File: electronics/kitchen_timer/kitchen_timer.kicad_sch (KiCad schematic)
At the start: 25 parts, among them J2 UART, J3 SWD, Q1 BC327, Q2 BC327, Q3 BC327, Q4 BC327, SW1 BTN_A, SW2 BTN_B, SW3 BTN_C, SW4 BTN_D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

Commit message: Add 3d models to components, small rerouting
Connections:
- net GND: now also U2.23 (GND), U2.28 (GND)
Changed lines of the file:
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@@
+	)
+	(junction
+		(at 121.92 64.77)
+		(diameter 0)
+		(color 0 0 0 0)
 	)
 	(junction
@@
 	)
 	(junction
+		(at 121.92 39.37)
+		(diameter 0)
+		(color 0 0 0 0)
+	)
+	(junction
 		(at 33.02 69.85)
 		(diameter 0)
@@
 	(wire
 		(pts
+			(xy 121.92 77.47) (xy 121.92 64.77)
+		)
+		(stroke
+			(width 0)
+			(type default)
+		)
+	)
+	(wire
+		(pts
 			(xy 39.37 69.85) (xy 45.72 69.85)
 		)
@@
 	(wire
 		(pts
+			(xy 121.92 64.77) (xy 121.92 39.37)
+		)
+		(stroke
+			(width 0)
+			(type default)
+		)
+	)
+	(wire
+		(pts
 			(xy 191.77 120.65) (xy 191.77 161.29)
 		)
@@
 	(wire
 		(pts
-			(xy 129.54 39.37) (xy 118.11 39.37)
+			(xy 129.54 39.37) (xy 121.92 39.37)
 		)
 		(stroke
@@
 	(wire
 		(pts
+			(xy 121.92 39.37) (xy 118.11 39.37)
+		)
+		(stroke
+			(width 0)
+			(type default)
+		)
+	)
+	(wire
+		(pts
 			(xy 106.68 157.48) (xy 106.68 181.61)
 		)
@@
 	(wire
 		(pts
+			(xy 118.11 77.47) (xy 121.92 77.47)
+		)
+		(stroke
+			(width 0)
+			(type default)
+		)
+	)
+	(wire
+		(pts
 			(xy 163.83 44.45) (xy 173.99 44.45)
 		)
@@
 		)
 		(stroke
+			(width 0)
+			(type default)
+		)
+	)
+	(wire
+		(pts
+			(xy 118.11 64.77) (xy 121.92 64.77)
+		)
+		(stroke

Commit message: Update electronics
- added Schottky diode and solder bridge
- corrected all errors from design rules checker
- added silk screen logos
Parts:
- added TP1: PWM_SPEAKER, TestPoint:TestPoint_Pad_2.0x2.0mm, symbol Connector:TestPoint
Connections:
- net GND: now also U2.13 (GND), U2.18 (GND), U2.8 (GND)
- net charging_and_audio/PWM_SPEAKER renamed PWM_SPEAKER
- net PWM_SPEAKER: now also TP1.1
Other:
- note added: "Testpoints"
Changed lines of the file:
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@@
 	)
 	(junction
+		(at 67.31 39.37)
+		(diameter 0)
+		(color 0 0 0 0)
+	)
+	(junction
 		(at 121.92 64.77)
 		(diameter 0)
@@
 	)
 	(junction
+		(at 80.01 64.77)
+		(diameter 0)
+		(color 0 0 0 0)
+	)
+	(junction
 		(at 121.92 39.37)
 		(diameter 0)
@@
 	)
 	(junction
+		(at 76.2 52.07)
+		(diameter 0)
+		(color 0 0 0 0)
+	)
+	(junction
 		(at 173.99 44.45)
 		(diameter 0)
@@
 	(wire
 		(pts
+			(xy 76.2 64.77) (xy 76.2 52.07)
+		)
+		(stroke
+			(width 0)
+			(type default)
+		)
+	)
+	(wire
+		(pts
 			(xy 95.25 116.84) (xy 119.38 116.84)
 		)
@@
 	(wire
 		(pts
+			(xy 76.2 52.07) (xy 67.31 52.07)
+		)
+		(stroke
+			(width 0)
+			(type default)
+		)
+	)
+	(wire
+		(pts
 			(xy 58.42 59.69) (xy 58.42 57.15)
 		)
@@
 	(wire
 		(pts
+			(xy 67.31 39.37) (xy 82.55 39.37)
+		)
+		(stroke
+			(width 0)
+			(type default)
+		)
+	)
+	(wire
+		(pts
 			(xy 101.6 99.06) (xy 101.6 138.43)
 		)
@@
 	(wire
 		(pts
-			(xy 118.11 54.61) (xy 146.05 54.61)
-		)
-		(stroke
-			(width 0)
-			(type default)
-		)
-	)
-	(wire
-		(pts
 			(xy 115.57 130.81) (xy 115.57 138.43)
 		)
@@
 	(wire
 		(pts
+			(xy 223.52 30.48) (xy 229.87 30.48)
+		)
+		(stroke
+			(width 0)
+			(type default)
+		)
+	)
+	(wire
+		(pts
 			(xy 73.66 172.72) (xy 82.55 172.72)
 		)
@@
 	(wire
 		(pts
+			(xy 80.01 64.77) (xy 76.2 64.77)
+		)
+		(stroke
+			(width 0)
+			(type default)
+		)
+	)
+	(wire
+		(pts
 			(xy 134.62 83.82) (xy 134.62 105.41)
 		)
@@
 	(wire
 		(pts
+			(xy 82.55 64.77) (xy 80.01 64.77)
+		)
+		(stroke
+			(width 0)
+			(type default)
+		)
+	)
+	(wire
+		(pts
+			(xy 80.01 77.47) (xy 80.01 64.77)
+		)
+		(stroke
+			(width 0)
+			(type default)
+		)
+	)
+	(wire
+		(pts
 			(xy 182.88 130.81) (xy 115.57 130.81)
 		)
@@
 	(wire
 		(pts
+			(xy 67.31 52.07) (xy 67.31 39.37)
+		)
+		(stroke
+			(width 0)
+			(type default)
+		)
+	)
+	(wire
+		(pts
 			(xy 182.88 44.45) (xy 182.88 100.33)
 		)
@@
 	(wire
 		(pts
+			(xy 118.11 54.61) (xy 157.48 54.61)
+		)
+		(stroke
+			(width 0)
+			(type default)
+		)
+	)
+	(wire
+		(pts
 			(xy 45.72 69.85) (xy 58.42 69.85)
 		)
@@
 	(wire
 		(pts
-			(xy 146.05 31.75) (xy 165.1 31.75)
+			(xy 157.48 31.75) (xy 165.1 31.75)
 		)
 		(stroke
@@
 	(wire
 		(pts
+			(xy 157.48 31.75) (xy 157.48 54.61)
+		)
+		(stroke
+			(width 0)
+			(type default)
+		)
+	)
+	(wire
+		(pts
 			(xy 66.04 59.69) (xy 66.04 92.71)
 		)
@@
 	(wire
 		(pts
-			(xy 66.04 92.71) (xy 44.45 92.71)
+			(xy 82.55 52.07) (xy 76.2 52.07)
 		)
 		(stroke
@@
 	(wire
 		(pts
-			(xy 39.37 69.85) (xy 39.37 77.47)
+			(xy 66.04 92.71) (xy 44.45 92.71)
 		)
 		(stroke
@@
 	(wire
 		(pts
-			(xy 146.05 54.61) (xy 146.05 31.75)
+			(xy 39.37 69.85) (xy 39.37 77.47)
 		)
 		(stroke
@@
 	(wire
 		(pts
+			(xy 82.55 77.47) (xy 80.01 77.47)
+		)
+		(stroke
+			(width 0)
+			(type default)
+		)
+	)
+	(wire
+		(pts
 			(xy 90.17 172.72) (xy 111.76 172.72)
 		)
@@
 	(wire
 		(pts
-			(xy 57.15 39.37) (xy 82.55 39.37)
+			(xy 57.15 39.37) (xy 67.31 39.37)
 		)
 		(stroke
@@
 	(wire
 		(pts
+			(xy 223.52 27.94) (xy 223.52 30.48)
+		)
+		(stroke
+			(width 0)
+			(type default)
+		)
+	)
+	(wire
+		(pts
 			(xy 33.02 49.53) (xy 33.02 59.69)
 		)
@@
 		)
 	)
+	(rectangle
+		(start 218.44 20.32)
+		(end 274.32 33.02)
+		(stroke
+			(width 0)
+			(type default)
+		)
+		(fill
+			(type color)
+			(color 255 255 175 1)
+		)
+	)
 	(image
 		(at 243.84 147.32)
@@
 		)
 	)
-	(text_box "TODO\n- Zener diode"
+	(text "Segments and digits:"
 		(exclude_from_sim no)
-		(at 215.9 85.09 0)
-		(size 54.61 25.4)
-		(stroke
-			(width 0)
-			(type default)
+		(at 244.348 132.842 0)
+		(effects
+			(font
+				(size 1.27 1.27)
+			)
 		)
-		(fill
-			(type color)
-			(color 255 255 175 1)
+	)
+	(text "Testpoints"
+		(exclude_from_sim no)
+		(at 245.11 18.034 0)
+		(effects
+			(font
+				(size 1.27 1.27)
+			)
 		)
+	)
+	(label "PWM_SPEAKER"
+		(at 229.87 30.48 0)
+		(fields_autoplaced yes)
 		(effects
 			(font
 				(size 1.27 1.27)
 			)
-			(justify left top)
+			(justify left bottom)
 		)
 	)
-	(text "Segments and digits:"
-		(exclude_from_sim no)
-		(at 244.348 132.842 0)
+	(label "PWM_SPEAKER"
+		(at 135.89 54.61 0)
+		(fields_autoplaced yes)
 		(effects
 			(font
 				(size 1.27 1.27)
 			)
+			(justify left bottom)
 		)
 	)
@@
 					(unit 1)
 				)
+			)
+		)
+	)
+	(symbol
+		(lib_id "Connector:TestPoint")
+		(at 223.52 27.94 0)
+		(unit 1)
+		(exclude_from_sim no)
+		(in_bom yes)
+		(on_board yes)
+		(dnp no)
+		(fields_autoplaced yes)
+		(property "Reference" "TP1"
+			(at 226.06 23.3679 0)
+			(effects
+				(font
+					(size 1.27 1.27)
+				)
+				(justify left)
+			)
+		)
+		(property "Value" "PWM_SPEAKER"
+			(at 226.06 25.9079 0)
+			(effects
+				(font
+					(size 1.27 1.27)
+				)
+				(justify left)
+			)
+		)
+		(property "Footprint" "TestPoint:TestPoint_Pad_2.0x2.0mm"
+			(at 228.6 27.94 0)
+			(effects
+				(font
+					(size 1.27 1.27)
+				)
+				(hide yes)
+			)
+		)
+		(property "Datasheet" "~"
+			(at 228.6 27.94 0)
+			(effects
+				(font
+					(size 1.27 1.27)
+				)
+				(hide yes)
+			)
+		)
+		(property "Description" "test point"
+			(at 223.52 27.94 0)
+			(effects
+				(font
+					(size 1.27 1.27)
+				)
+				(hide yes)
+			)
+		)
+		(pin "1"
+		)
+		(instances
+			(project ""
+				(path "/10a34ff8-9938-4755-8ae4-3799cb1684e2"
+					(reference "TP1")
+					(unit 1)
+				)

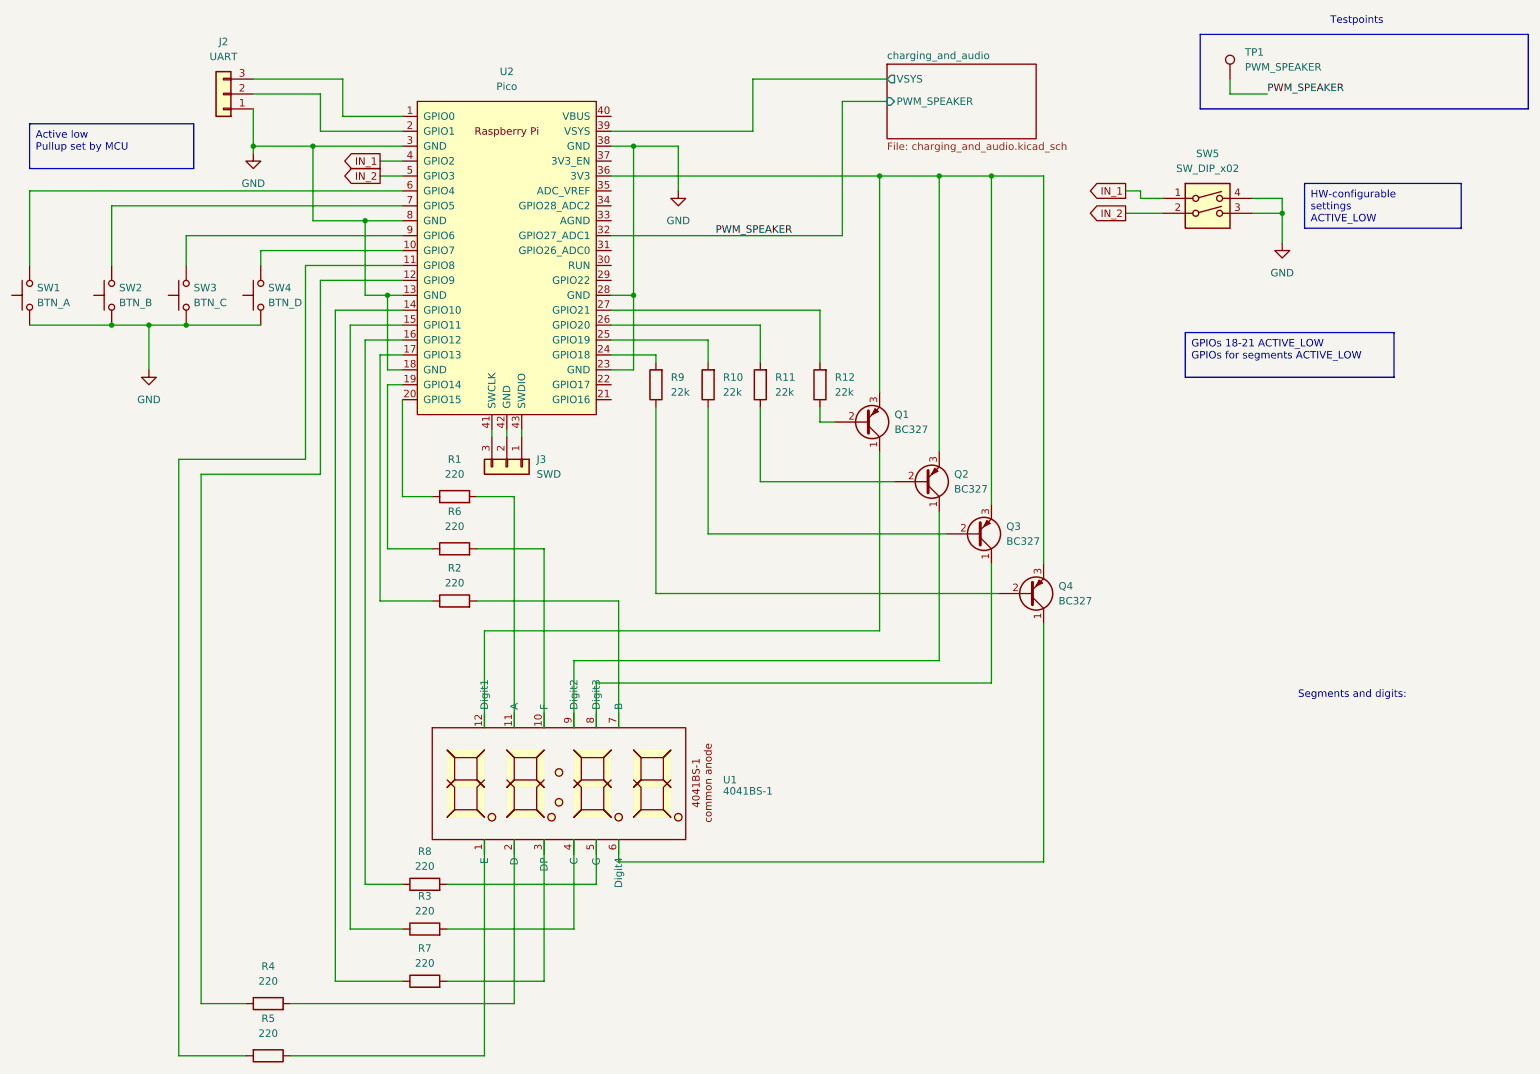
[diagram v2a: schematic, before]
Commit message: Update electronics
- resistors with longer spacing between holes
- GND for SWD
- solder jumper new footprint
- increase distances between nets

- added datasheet for schottky
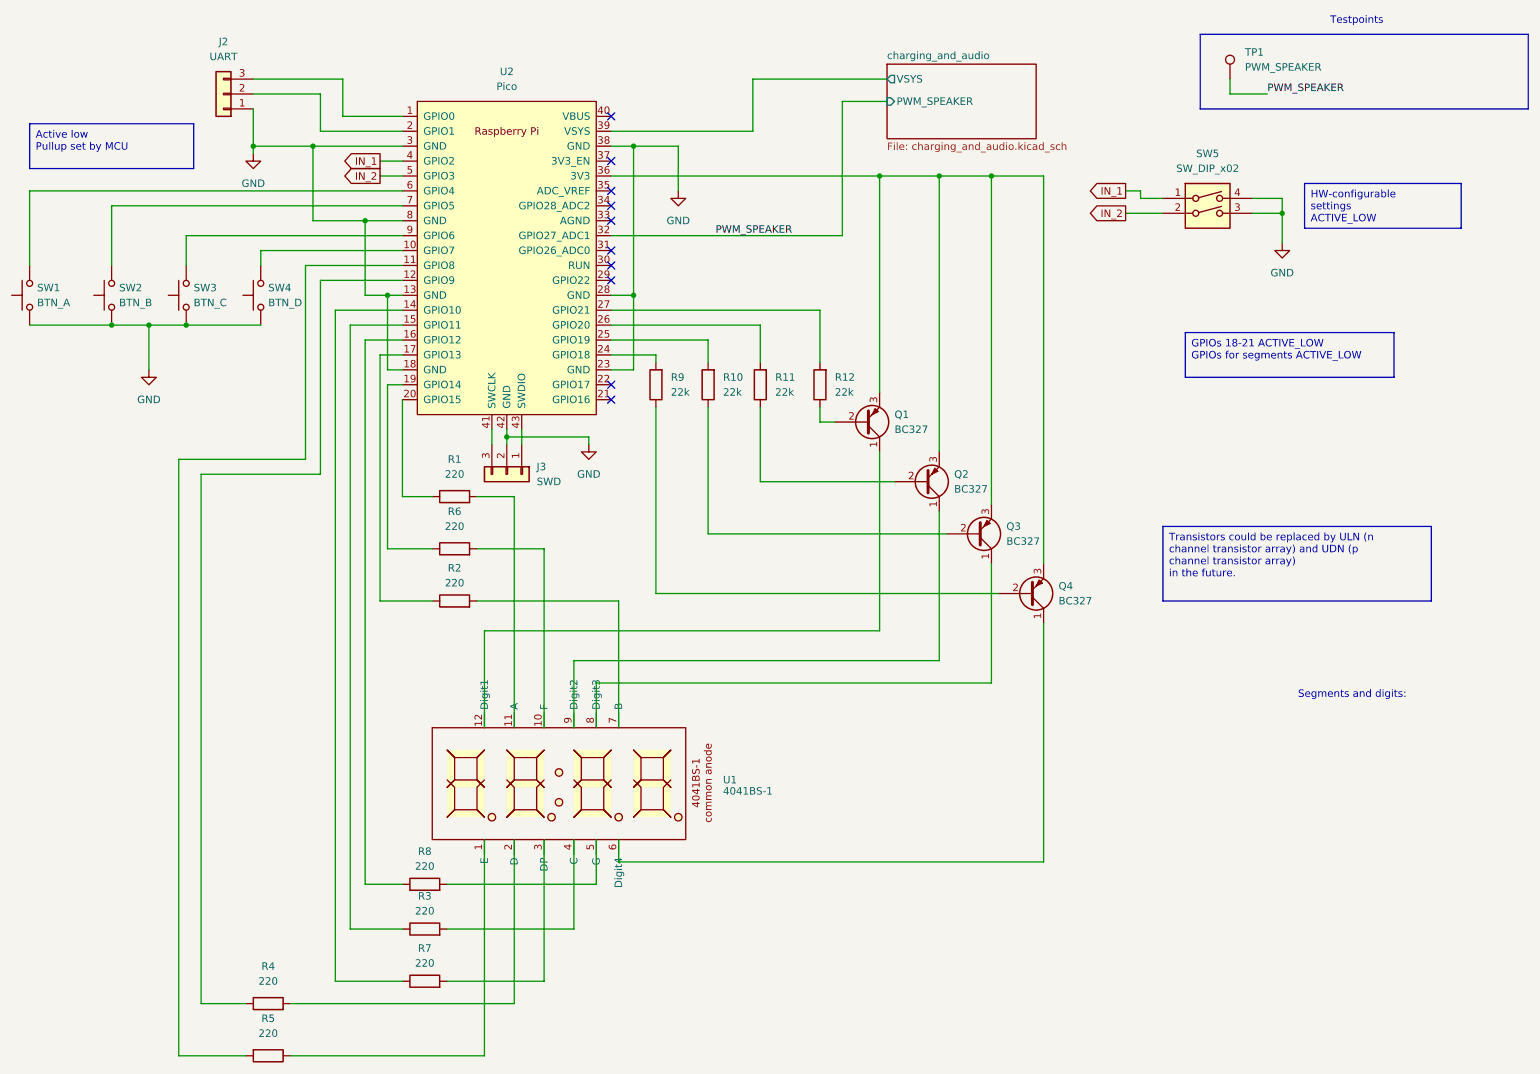
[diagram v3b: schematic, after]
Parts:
- R1, R10, R11, R12, R2, R3, R4, R5, R6, R7, R8, R9: footprint Resistor_THT:R_Axial_DIN0207_L6.3mm_D2.5mm_P7.62mm_Horizontal -> Resistor_THT:R_Axial_DIN0207_L6.3mm_D2.5mm_P10.16mm_Horizontal
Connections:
- net GND: now also J3.2 (Pin_2), U2.42 (GND)
- no-connect marks 0 -> 10
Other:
- moved on the sheet: J3
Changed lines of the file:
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@@
 	)
 	(junction
+		(at 100.33 88.9)
+		(diameter 0)
+		(color 0 0 0 0)
+	)
+	(junction
 		(at 39.37 69.85)
 		(diameter 0)
 		(color 0 0 0 0)
 	)
+	(no_connect
+		(at 118.11 82.55)
+	)
+	(no_connect
+		(at 118.11 62.23)
+	)
+	(no_connect
+		(at 118.11 46.99)
+	)
+	(no_connect
+		(at 118.11 57.15)
+	)
+	(no_connect
+		(at 118.11 59.69)
+	)
+	(no_connect
+		(at 118.11 34.29)
+	)
+	(no_connect
+		(at 118.11 52.07)
+	)
+	(no_connect
+		(at 118.11 80.01)
+	)
+	(no_connect
+		(at 118.11 41.91)
+	)
+	(no_connect
+		(at 118.11 49.53)
+	)
 	(wire
 		(pts
@@
 	(wire
 		(pts
+			(xy 114.3 90.17) (xy 114.3 88.9)
+		)
+		(stroke
+			(width 0)
+			(type default)
+		)
+	)
+	(wire
+		(pts
 			(xy 58.42 59.69) (xy 58.42 57.15)
 		)
@@
 	(wire
 		(pts
-			(xy 97.79 87.63) (xy 97.79 88.9)
+			(xy 97.79 87.63) (xy 97.79 90.17)
 		)
 		(stroke
@@
 	(wire
 		(pts
+			(xy 100.33 88.9) (xy 100.33 90.17)
+		)
+		(stroke
+			(width 0)
+			(type default)
+		)
+	)
+	(wire
+		(pts
 			(xy 82.55 62.23) (xy 68.58 62.23)
 		)
@@
 	(wire
 		(pts
-			(xy 102.87 87.63) (xy 102.87 88.9)
+			(xy 102.87 87.63) (xy 102.87 90.17)
 		)
 		(stroke
@@
 	(wire
 		(pts
+			(xy 114.3 88.9) (xy 100.33 88.9)
+		)
+		(stroke
+			(width 0)
+			(type default)
+		)
+	)
+	(wire
+		(pts
 			(xy 57.15 39.37) (xy 67.31 39.37)
 		)
@@
 		)
 	)
+	(text_box "Transistors could be replaced by ULN (n channel transistor array) and UDN (p channel transistor array)\nin the future."
+		(exclude_from_sim no)
+		(at 212.09 104.14 0)
+		(size 45.72 12.7)
+		(stroke
+			(width 0)
+			(type default)
+		)
+		(fill
+			(type color)
+			(color 255 247 192 1)
+		)
+		(effects
+			(font
+				(size 1.27 1.27)
+			)
+			(justify left top)
+		)
+	)
 	(text_box "HW-configurable settings\nACTIVE_LOW"
 		(exclude_from_sim no)
@@
 			)
 		)
-		(property "Footprint" "Resistor_THT:R_Axial_DIN0207_L6.3mm_D2.5mm_P7.62mm_Horizontal"
+		(property "Footprint" "Resistor_THT:R_Axial_DIN0207_L6.3mm_D2.5mm_P10.16mm_Horizontal"
 			(at 91.44 118.618 90)
 			(effects
@@
 	(symbol
 		(lib_id "Connector_Generic:Conn_01x03")
-		(at 100.33 93.98 270)
+		(at 100.33 95.25 270)
 		(unit 1)
 		(exclude_from_sim no)
@@
 		(fields_autoplaced yes)
 		(property "Reference" "J3"
-			(at 105.41 92.7099 90)
+			(at 105.41 93.9799 90)
 			(effects
 				(font
@@
 		)
 		(property "Value" "SWD"
-			(at 105.41 95.2499 90)
+			(at 105.41 96.5199 90)
 			(effects
 				(font
@@
 		)
 		(property "Footprint" "Connector_PinSocket_2.54mm:PinSocket_1x03_P2.54mm_Horizontal"
-			(at 100.33 93.98 0)
+			(at 100.33 95.25 0)
 			(effects
 				(font
@@
 		)
 		(property "Datasheet" "~"
-			(at 100.33 93.98 0)
+			(at 100.33 95.25 0)
 			(effects
 				(font
@@
 		)
 		(property "Description" "Generic connector, single row, 01x03, script generated (kicad-library-utils/schlib/autogen/connector/)"
-			(at 100.33 93.98 0)
+			(at 100.33 95.25 0)
 			(effects
 				(font
@@
 			)
 		)
-		(property "Footprint" "Resistor_THT:R_Axial_DIN0207_L6.3mm_D2.5mm_P7.62mm_Horizontal"
+		(property "Footprint" "Resistor_THT:R_Axial_DIN0207_L6.3mm_D2.5mm_P10.16mm_Horizontal"
 			(at 59.69 192.532 90)
 			(effects
@@
 			)
 		)
-		(property "Footprint" "Resistor_THT:R_Axial_DIN0207_L6.3mm_D2.5mm_P7.62mm_Horizontal"
+		(property "Footprint" "Resistor_THT:R_Axial_DIN0207_L6.3mm_D2.5mm_P10.16mm_Horizontal"
 			(at 91.44 100.838 90)
 			(effects
@@
 			)
 		)
-		(property "Footprint" "Resistor_THT:R_Axial_DIN0207_L6.3mm_D2.5mm_P7.62mm_Horizontal"
+		(property "Footprint" "Resistor_THT:R_Axial_DIN0207_L6.3mm_D2.5mm_P10.16mm_Horizontal"
 			(at 91.44 109.728 90)
 			(effects
@@
 			)
 		)
-		(property "Footprint" "Resistor_THT:R_Axial_DIN0207_L6.3mm_D2.5mm_P7.62mm_Horizontal"
+		(property "Footprint" "Resistor_THT:R_Axial_DIN0207_L6.3mm_D2.5mm_P10.16mm_Horizontal"
 			(at 86.36 183.388 90)
 			(effects
@@
 			)
 		)
-		(property "Footprint" "Resistor_THT:R_Axial_DIN0207_L6.3mm_D2.5mm_P7.62mm_Horizontal"
+		(property "Footprint" "Resistor_THT:R_Axial_DIN0207_L6.3mm_D2.5mm_P10.16mm_Horizontal"
 			(at 86.36 174.498 90)
 			(effects
@@
 			)
 		)
-		(property "Footprint" "Resistor_THT:R_Axial_DIN0207_L6.3mm_D2.5mm_P7.62mm_Horizontal"
+		(property "Footprint" "Resistor_THT:R_Axial_DIN0207_L6.3mm_D2.5mm_P10.16mm_Horizontal"
 			(at 155.448 80.01 90)
 			(effects
@@
 			)
 		)
-		(property "Footprint" "Resistor_THT:R_Axial_DIN0207_L6.3mm_D2.5mm_P7.62mm_Horizontal"
+		(property "Footprint" "Resistor_THT:R_Axial_DIN0207_L6.3mm_D2.5mm_P10.16mm_Horizontal"
 			(at 145.288 80.01 90)
 			(effects
@@
 			)
 		)
-		(property "Footprint" "Resistor_THT:R_Axial_DIN0207_L6.3mm_D2.5mm_P7.62mm_Horizontal"
+		(property "Footprint" "Resistor_THT:R_Axial_DIN0207_L6.3mm_D2.5mm_P10.16mm_Horizontal"
 			(at 127.508 80.01 90)
 			(effects
@@
 			)
 		)
-		(property "Footprint" "Resistor_THT:R_Axial_DIN0207_L6.3mm_D2.5mm_P7.62mm_Horizontal"
+		(property "Footprint" "Resistor_THT:R_Axial_DIN0207_L6.3mm_D2.5mm_P10.16mm_Horizontal"
 			(at 86.36 166.878 90)
 			(effects
@@
 	)
 	(symbol
+		(lib_id "power:GND")
+		(at 114.3 90.17 0)
+		(unit 1)
+		(exclude_from_sim no)
+		(in_bom yes)
+		(on_board yes)
+		(dnp no)
+		(fields_autoplaced yes)
+		(property "Reference" "#PWR08"
+			(at 114.3 96.52 0)
+			(effects
+				(font
+					(size 1.27 1.27)
+				)
+				(hide yes)
+			)
+		)
+		(property "Value" "GND"
+			(at 114.3 95.25 0)
+			(effects
+				(font
+					(size 1.27 1.27)
+				)
+			)
+		)
+		(property "Footprint" ""
+			(at 114.3 90.17 0)
+			(effects
+				(font
+					(size 1.27 1.27)
+				)
+				(hide yes)
+			)
+		)
+		(property "Datasheet" ""
+			(at 114.3 90.17 0)
+			(effects
+				(font
+					(size 1.27 1.27)
+				)
+				(hide yes)
+			)
+		)
+		(property "Description" "Power symbol creates a global label with name \"GND\" , ground"
+			(at 114.3 90.17 0)
+			(effects
+				(font
+					(size 1.27 1.27)
+				)
+				(hide yes)
+			)
+		)
+		(pin "1"
+		)
+		(instances
+			(project "kitchen_timer"
+				(path "/10a34ff8-9938-4755-8ae4-3799cb1684e2"
+					(reference "#PWR08")
+					(unit 1)
+				)
+			)
+		)
+	)
+	(symbol
 		(lib_id "Device:R")
 		(at 134.62 80.01 180)
@@
 			)
 		)
-		(property "Footprint" "Resistor_THT:R_Axial_DIN0207_L6.3mm_D2.5mm_P7.62mm_Horizontal"
+		(property "Footprint" "Resistor_THT:R_Axial_DIN0207_L6.3mm_D2.5mm_P10.16mm_Horizontal"
 			(at 136.398 80.01 90)
 			(effects
@@
 			)
 		)
-		(property "Footprint" "Resistor_THT:R_Axial_DIN0207_L6.3mm_D2.5mm_P7.62mm_Horizontal"
+		(property "Footprint" "Resistor_THT:R_Axial_DIN0207_L6.3mm_D2.5mm_P10.16mm_Horizontal"
 			(at 59.69 187.198 90)
 			(effects
